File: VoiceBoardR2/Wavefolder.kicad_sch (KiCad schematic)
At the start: 48 parts, among them Q401 BC858, Q402 BC857, Q403 BC847, Q404 BC857, Q405 BC847, Q406 BC858, U402 LM13700, U403 TL074, U404 TL074

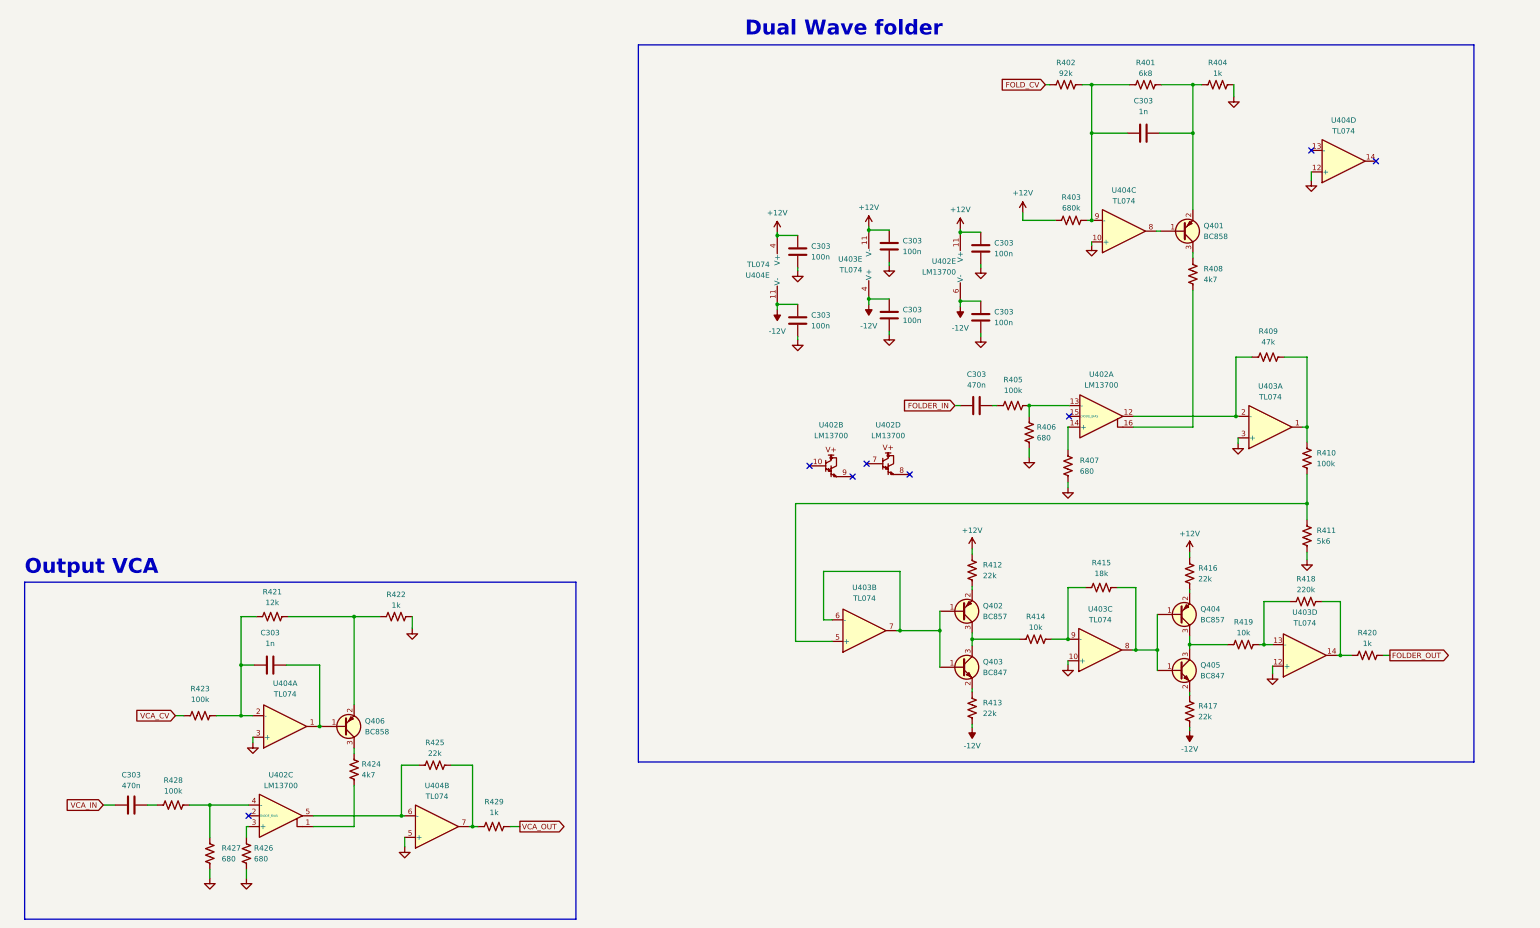
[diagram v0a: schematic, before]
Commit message: filter simulation
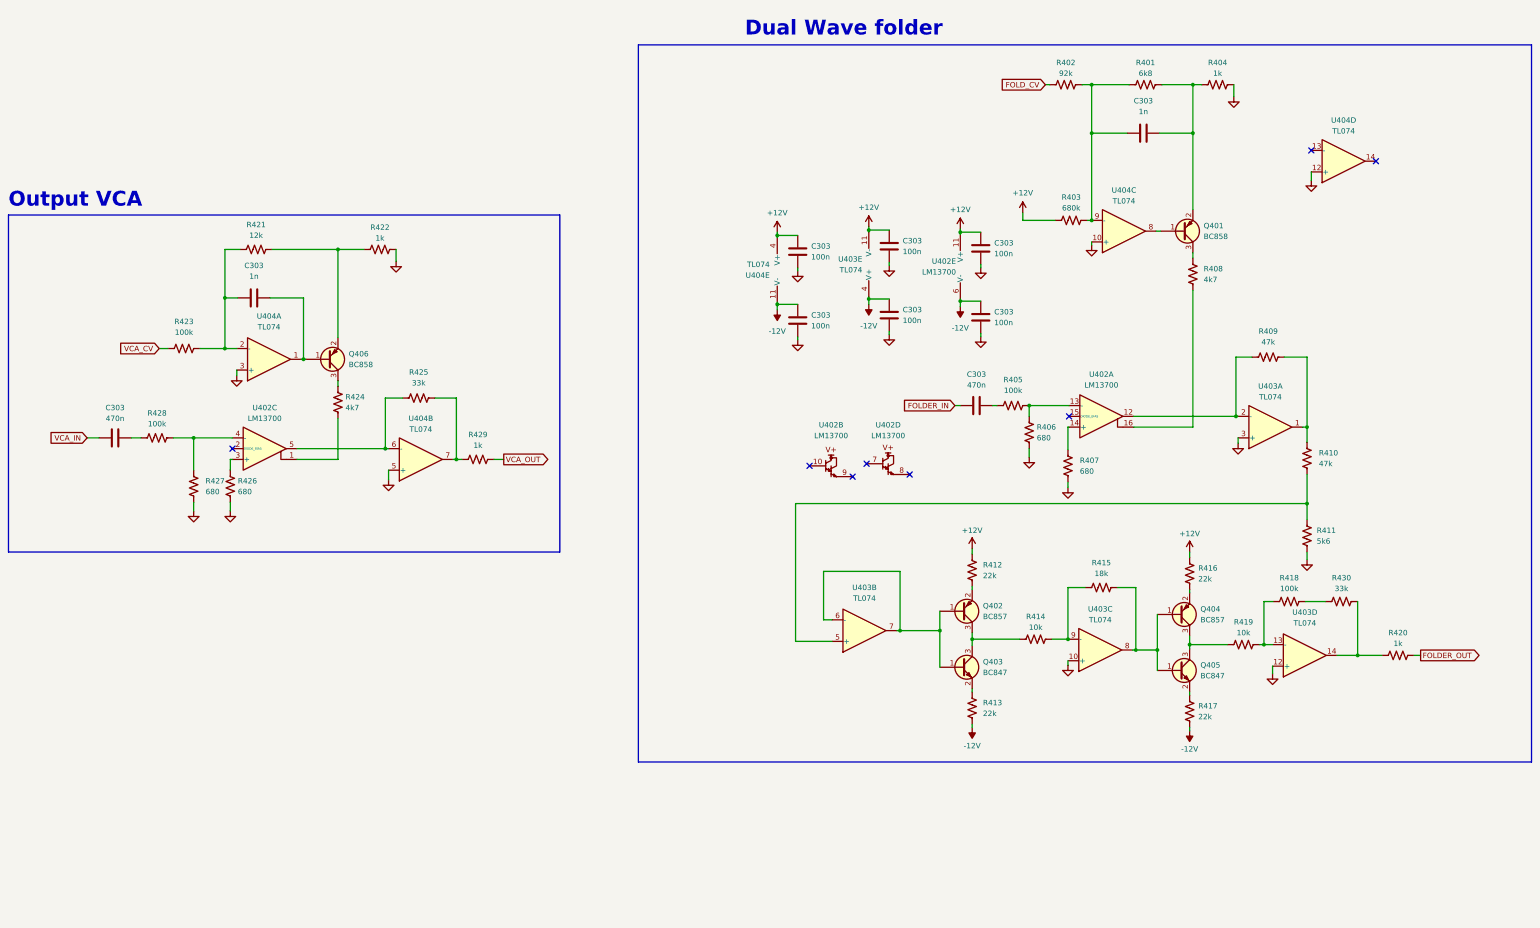
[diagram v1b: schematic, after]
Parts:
- added R430: 33k, PCM_Resistor_SMD_AKL:R_0805_2012Metric, symbol Device:R_US
- R410: value 100k -> 47k
- R418: value 220k -> 100k
- R425: value 22k -> 33k
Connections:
- net at R420.2, U403.14: now also R430.1; no longer R418.1
- new net: R418.1, R430.2
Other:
- moved on the sheet: C303, Q406, R418, R420, R421, R422, R423, R424, R425, R426, R427, R428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

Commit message: fixed git maybe
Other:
- note added: "NOTE: POWER PINS BACKWARD!!!"
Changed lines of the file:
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@@
     (fill (type none))
   )
-  (text "Dual Wave folder" (at 193.548 47.752 0)
+  (text "NOTE: POWER PINS BACKWARD!!!" (at 208.788 86.487 0)
+    (effects (font (size 1.27 1.27)) (justify left bottom))
+  )
+  (text "Dual Wave folder" (at 168.275 46.863 0)
     (effects (font (face "KiCad Font") (size 3.5 3.5) (thickness 0.7) bold) (justify left bottom))
   )
